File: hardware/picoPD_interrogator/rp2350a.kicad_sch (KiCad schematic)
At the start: 0 parts

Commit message: Added most of the RP2350A parts.
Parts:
- added C10, C11, C12: 4.7uF, Capacitor_SMD:C_0603_1608Metric, symbol Device:C
- added C13, C14, C15, C16, C17, C18, C19, C20, C21, C22: 100nF, Capacitor_SMD:C_0201_0603Metric, symbol Device:C
- added C8, C9: 15pF, Capacitor_SMD:C_0201_0603Metric, symbol Device:C
- added L2: 3.3uH, picoPD_interrogator:L_pol_2016, symbol Device:L
- added Q6: rohm-RE1C002UN, Package_TO_SOT_SMD:SOT-416, symbol picoPD_interrogator:rohm-RE1C002UN
- added R26, R27, R28, R29: 1K, Resistor_SMD:R_0201_0603Metric, symbol Device:R
- added R30, R31: 27R, Resistor_SMD:R_0201_0603Metric, symbol Device:R
- added R32: 33R, Resistor_SMD:R_0201_0603Metric, symbol Device:R
- added SW1, SW2: SW_Push, symbol Switch:SW_Push
- added U10: RP2350_60QFN, picoPD_interrogator:RP2350-QFN-60-1EP_7x7_P0.4mm_EP3.4x3.4mm_ThermalVias, symbol picoPD_interrogator:RP2350_60QFN
- added U11: W25Q128JVS, Package_SO:SOIC-8_5.23x5.23mm_P1.27mm, symbol Memory_Flash:W25Q128JVS
- added Y1: Crystal_GND24, Crystal:Crystal_SMD_Abracon_ABM10-4Pin_2.5x2.0mm, symbol Device:Crystal_GND24
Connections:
- new net: R31.2, U10.51 (USB_DM)
- new net: R30.2, U10.52 (USB_DP)
- new net: Q6.2 (S), R29.1, SW2.1
- new net: C8.1, R26.2, Y1.3
- new net: R27.1, SW1.1
- new net 1V1: C11.1, C13.1, C14.1, C15.1, L2.1, U10.23 (DVDD), U10.39 (DVDD), U10.50 (VREG_FB), U10.6 (DVDD)
- new net 3V3: C10.1, C16.1, C17.1, C18.1, C19.1, C20.1, C21.1, C22.1, R32.1, U10.1 (IOVDD), U10.11 (IOVDD), U10.20 (IOVDD), U10.30 (IOVDD), U10.38 (IOVDD), U10.44 (ADC_AVDD), U10.45 (IOVDD), U10.49 (VREG_VIN), U10.53 (USB_OTP_VDD), U10.54 (QSPI_IOVDD), U11.8 (VCC)
- new net 3V3_SMOOTHED: C12.1, R32.2, U10.46 (VREG_AVDD)
- new net FLASH_CLK: U10.56 (QSPI_SCLK), U11.6 (CLK)
- new net FLASH_DISABLE_L: R27.2, U10.60 (QSPI_SS), U11.1 (~{CS})
- new net FLASH_SD0: U10.57 (QSPI_SD0), U11.5 (DI(IO0))
- new net FLASH_SD1: U10.59 (QSPI_SD1), U11.2 (DO(IO1))
- new net FLASH_SD2: U10.58 (QSPI_SD2), U11.3 (IO2)
- new net FLASH_SD3: U10.55 (QSPI_SD3), U11.7 (IO3)
- new net GND: C10.2, C11.2, C12.2, C13.2, C14.2, C15.2, C16.2, C17.2, C18.2, C19.2, C20.2, C21.2, C22.2, C8.2, C9.2, R28.2, R29.2, SW1.2, U10.47 (VREG_PGND), U10.61 (GND), U11.4 (GND), Y1.4
- new net GP0: U10.2 (GPIO0)
- new net GP1: U10.3 (GPIO1)
- new net GP10: U10.14 (GPIO10)
- new net GP11: U10.15 (GPIO11)
- new net GP12: U10.16 (GPIO12)
- new net GP13: U10.17 (GPIO13)
- new net GP14: U10.18 (GPIO14)
- new net GP15: U10.19 (GPIO15)
- new net GP16: U10.27 (GPIO16)
- new net GP17: U10.28 (GPIO17)
- new net GP18: U10.29 (GPIO18)
- new net GP19: U10.31 (GPIO19)
- new net GP2: U10.4 (GPIO2)
- new net GP20: U10.32 (GPIO20)
- new net GP21: U10.33 (GPIO21)
- new net GP22: U10.34 (GPIO22)
- new net GP23: U10.35 (GPIO23)
- new net GP24: U10.36 (GPIO24)
- new net GP25: U10.37 (GPIO25)
- new net GP26_ADC0: U10.40 (GPIO26_ADC0)
- new net GP27_ADC1: U10.41 (GPIO27_ADC1)
- new net GP28_ADC2: U10.42 (GPIO28_ADC2)
- new net GP29_ADC3: U10.43 (GPIO29_ADC3)
- new net GP3: U10.5 (GPIO3)
- new net GP4: U10.7 (GPIO4)
- new net GP5: U10.8 (GPIO5)
- new net GP6: U10.9 (GPIO6)
- new net GP7: U10.10 (GPIO7)
- new net GP8: U10.12 (GPIO8)
- new net GP9: U10.13 (GPIO9)
- new net MCU_RESET_L: Q6.3 (D), SW2.2, U10.26 (RUN)
- new net RP2_RESET: Q6.1 (G), R28.1
- new net SWD_CLK: U10.24 (SWCLK)
- new net SWD_IO: U10.25 (SWD)
- new net USB_DM: R31.1
- new net USB_DP: R30.1
- new net VREG_LX: L2.2, U10.48 (VREG_LX)
- new net XIN: C9.1, U10.21 (XIN), Y1.1
- new net XOUT: R26.1, U10.22 (XOUT)
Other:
- note added: "RP2 Reset Button"
- note added: "USB Bootloader Button"

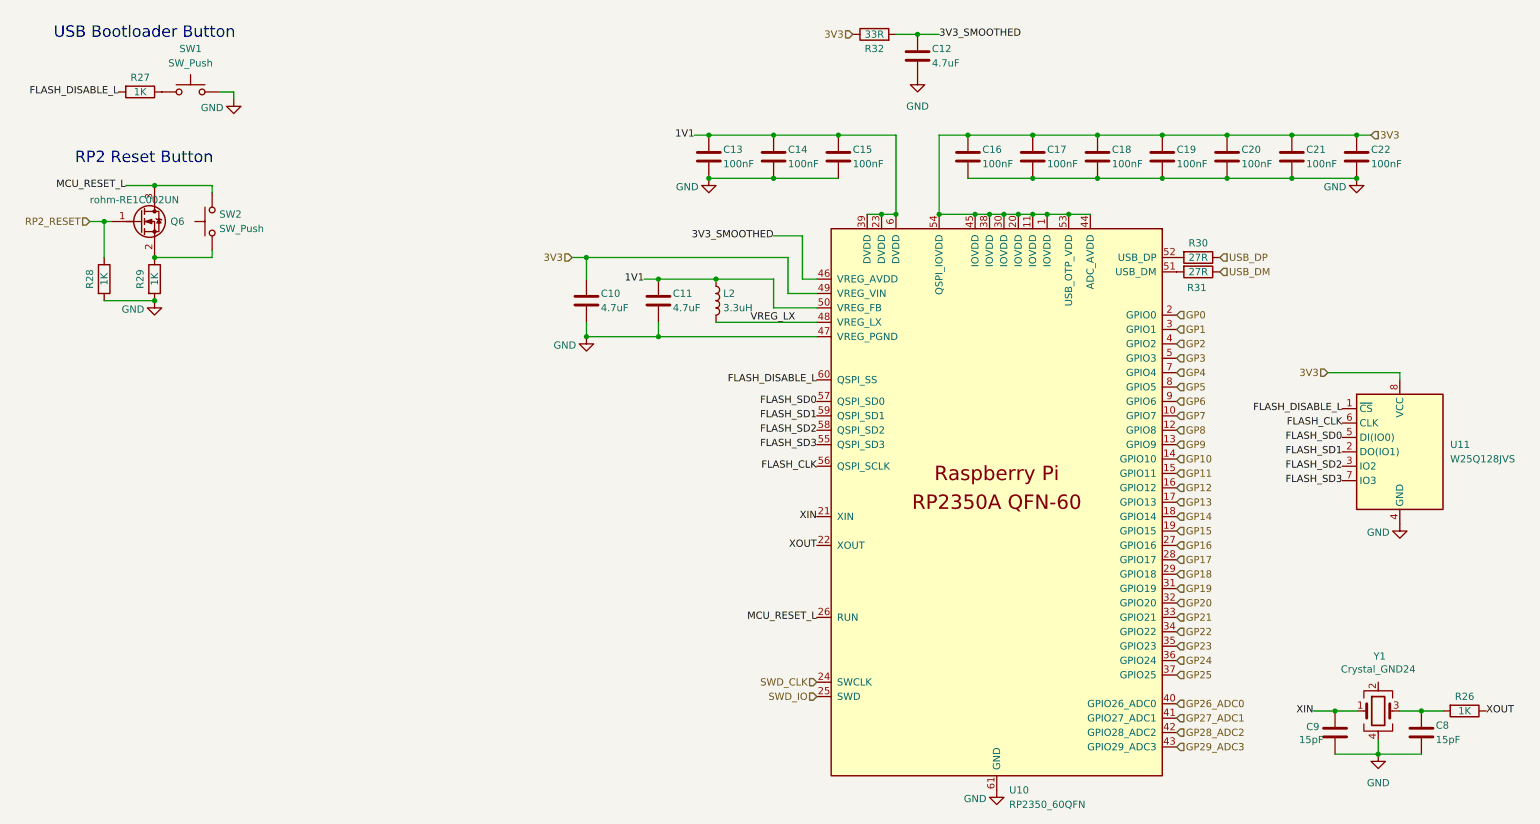
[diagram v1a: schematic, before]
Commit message: Schematic: Added QWIIC Connector. Changed 56K Rp resistor to 35K since we are pulling up 3.3v instead of 5v.
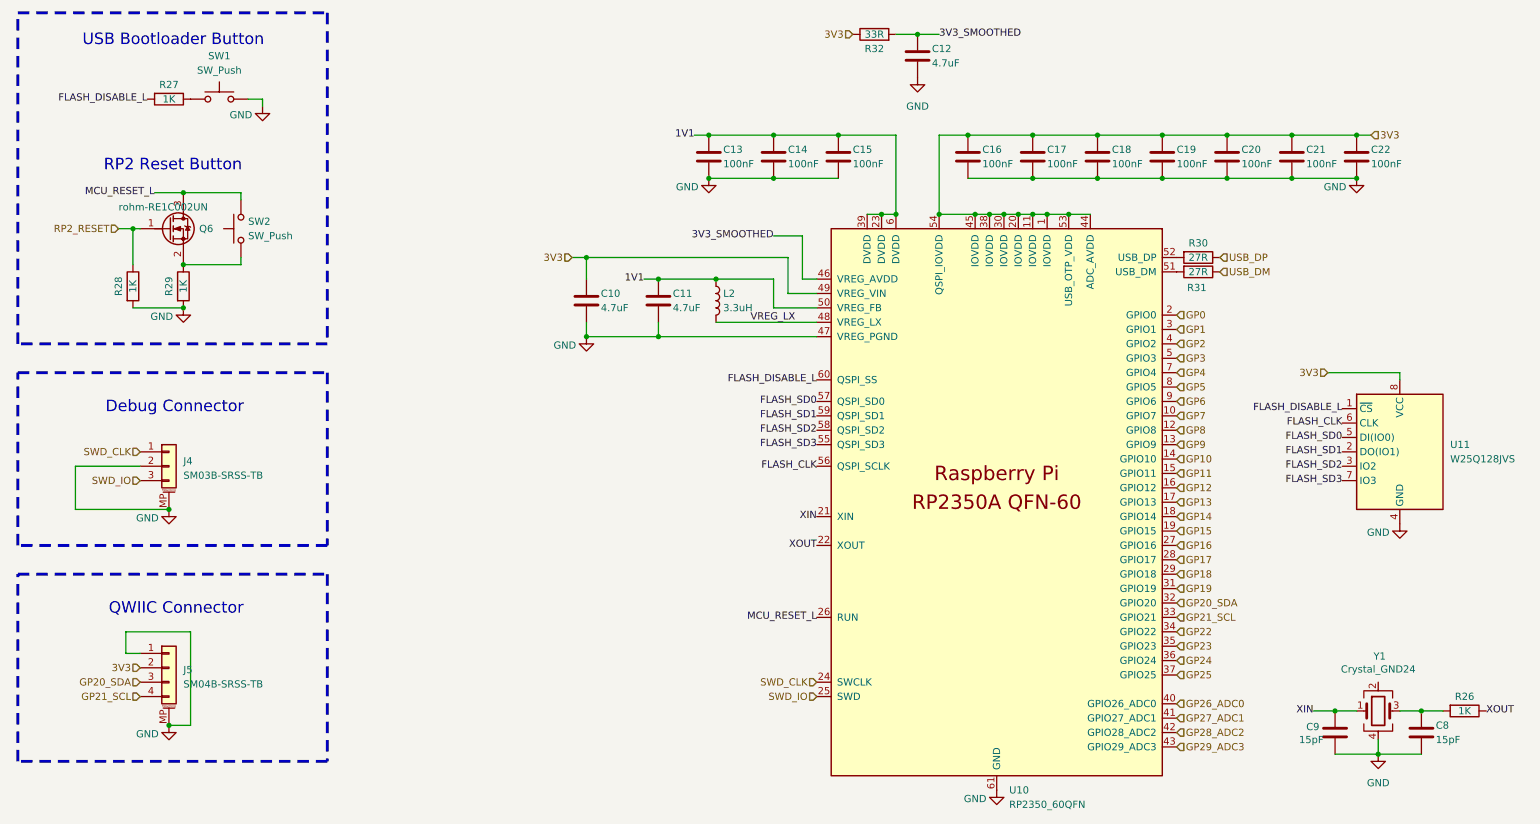
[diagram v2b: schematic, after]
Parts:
- added J4: SM03B-SRSS-TB, Connector_JST:JST_SH_SM03B-SRSS-TB_1x03-1MP_P1.00mm_Horizontal, symbol Connector_Generic_MountingPin:Conn_01x03_MountingPin
- added J5: SM04B-SRSS-TB, Connector_JST:JST_SH_SM04B-SRSS-TB_1x04-1MP_P1.00mm_Horizontal, symbol Connector_Generic_MountingPin:Conn_01x04_MountingPin
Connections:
- net 3V3: now also J5.2 (Pin_2)
- net GND: now also J4.2 (Pin_2), J4.MP (MountPin), J5.1 (Pin_1), J5.MP (MountPin)
- net SWD_CLK: now also J4.1 (Pin_1)
- net SWD_IO: now also J4.3 (Pin_3)
- net GP20 renamed GP20_SDA
- net GP20_SDA: now also J5.3 (Pin_3)
- net GP21 renamed GP21_SCL
- net GP21_SCL: now also J5.4 (Pin_4)
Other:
- note added: "Debug Connector"
- note added: "QWIIC Connector"
- moved on the sheet: Q6, R27, R28, R29, SW1, SW2

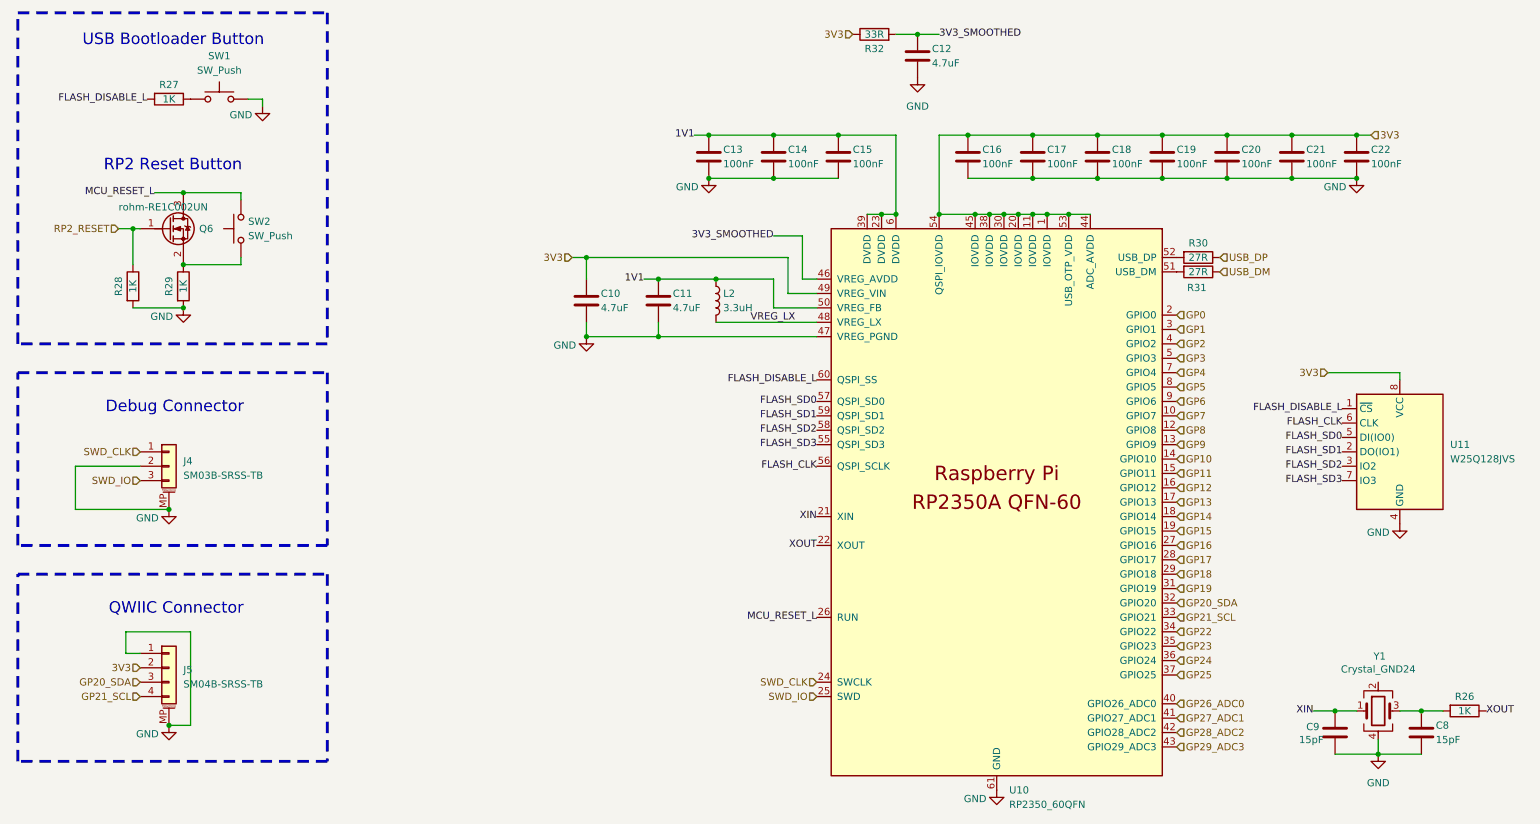
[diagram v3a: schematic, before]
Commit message: Schematic: Added an 'Extra Pins' connector.
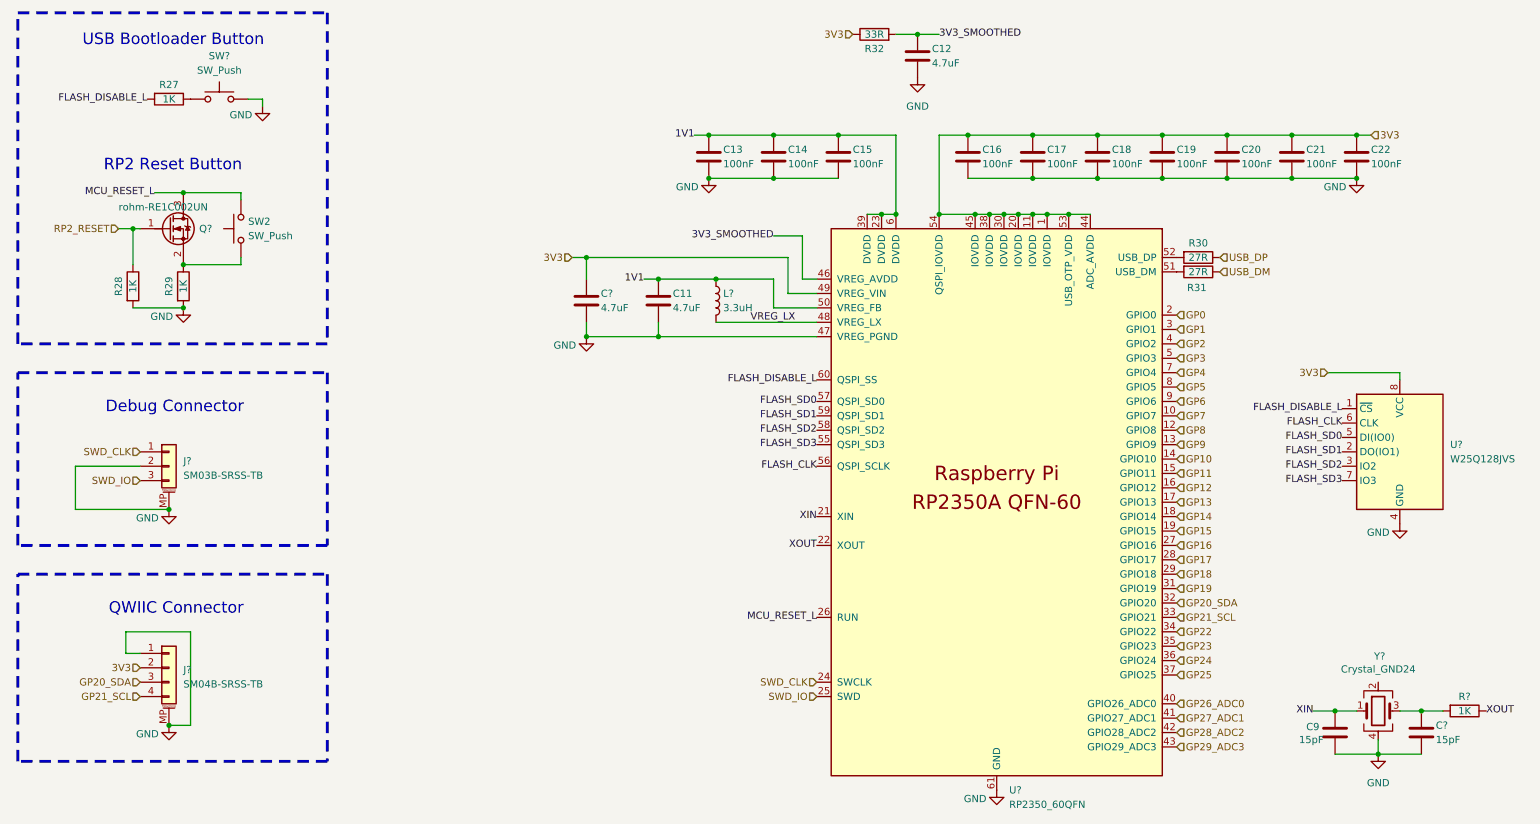
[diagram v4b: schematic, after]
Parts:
- renumbered C8 to C?, C10 to C?, J4 to J?, J5 to J?, L2 to L?, Q6 to Q?, R26 to R?, SW1 to SW?, U10 to U?, U11 to U?, Y1 to Y?
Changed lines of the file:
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@@
 		(dnp no)
 		(fields_autoplaced yes)
-		(property "Reference" "U10"
+		(property "Reference" "U?"
 			(at 191.4241 153.67 0)
 			(effects
@@
 		(pin "60"
 		)
+		(instances
+			(project "picoPD_interrogator"
+				(path "/e34b0978-7def-4921-94d0-accc0a677529/dcdf1db7-f9f6-495b-a623-7e4b73e77f06"
+					(reference "U?")
+					(unit 1)
+				)
+			)
+		)
 	)
 	(symbol
@@
 		(dnp no)
 		(fields_autoplaced yes)
-		(property "Reference" "U11"
+		(property "Reference" "U?"
 			(at 269.24 92.7099 0)
 			(effects
@@
 		(pin "7"
 		)
+		(instances
+			(project "picoPD_interrogator"
+				(path "/e34b0978-7def-4921-94d0-accc0a677529/dcdf1db7-f9f6-495b-a623-7e4b73e77f06"
+					(reference "U?")
+					(unit 1)
+				)
+			)
+		)
 	)
 	(symbol
@@
 		(on_board yes)
 		(dnp no)
-		(property "Reference" "Y1"
+		(property "Reference" "Y?"
 			(at 256.794 130.048 0)
 			(effects
@@
 		(pin "3"
 		)
+		(instances
+			(project "picoPD_interrogator"
+				(path "/e34b0978-7def-4921-94d0-accc0a677529/dcdf1db7-f9f6-495b-a623-7e4b73e77f06"
+					(reference "Y?")
+					(unit 1)
+				)
+			)
+		)
 	)
 	(symbol
@@
 		(dnp no)
 		(fields_autoplaced yes)
-		(property "Reference" "#PWR036"
+		(property "Reference" "#PWR?"
 			(at 175.26 34.29 0)
 			(effects
@@
 		(pin "1"
 		)
+		(instances
+			(project "picoPD_interrogator"
+				(path "/e34b0978-7def-4921-94d0-accc0a677529/dcdf1db7-f9f6-495b-a623-7e4b73e77f06"
+					(reference "#PWR?")
+					(unit 1)
+				)
+			)
+		)
 	)
 	(symbol
@@
 		(dnp no)
 		(fields_autoplaced yes)
-		(property "Reference" "#PWR031"
+		(property "Reference" "#PWR?"
 			(at 256.54 153.67 0)
 			(effects
@@
 		(pin "1"
 		)
+		(instances
+			(project "picoPD_interrogator"
+				(path "/e34b0978-7def-4921-94d0-accc0a677529/dcdf1db7-f9f6-495b-a623-7e4b73e77f06"
+					(reference "#PWR?")
+					(unit 1)
+				)
+			)
+		)
 	)
 	(symbol
@@
 		(dnp no)
 		(fields_autoplaced yes)
-		(property "Reference" "SW1"
+		(property "Reference" "SW?"
 			(at 52.07 24.13 0)
 			(effects
@@
 		(pin "2"
 		)
+		(instances
+			(project "picoPD_interrogator"
+				(path "/e34b0978-7def-4921-94d0-accc0a677529/dcdf1db7-f9f6-495b-a623-7e4b73e77f06"
+					(reference "SW?")
+					(unit 1)
+				)
+			)
+		)
 	)
 	(symbol
@@
 		(dnp no)
 		(fields_autoplaced yes)
-		(property "Reference" "J4"
+		(property "Reference" "J?"
 			(at 45.72 95.6055 0)
 			(effects
@@
 		(pin "2"
 		)
+		(instances
+			(project "picoPD_interrogator"
+				(path "/e34b0978-7def-4921-94d0-accc0a677529/dcdf1db7-f9f6-495b-a623-7e4b73e77f06"
+					(reference "J?")
+					(unit 1)
+				)
+			)
+		)
 	)
 	(symbol
@@
 		(on_board yes)
 		(dnp no)
-		(property "Reference" "#PWR032"
+		(property "Reference" "#PWR?"
 			(at 59.69 39.37 0)
 			(effects
@@
 		(pin "1"
 		)
+		(instances
+			(project "picoPD_interrogator"
+				(path "/e34b0978-7def-4921-94d0-accc0a677529/dcdf1db7-f9f6-495b-a623-7e4b73e77f06"
+					(reference "#PWR?")
+					(unit 1)
+				)
+			)
+		)
 	)
 	(symbol
@@
 		(on_board yes)
 		(dnp no)
-		(property "Reference" "C8"
+		(property "Reference" "C?"
 			(at 266.7 142.24 0)
 			(effects
@@
 		(pin "2"
 		)
+		(instances
+			(project "picoPD_interrogator"
+				(path "/e34b0978-7def-4921-94d0-accc0a677529/dcdf1db7-f9f6-495b-a623-7e4b73e77f06"
+					(reference "C?")
+					(unit 1)
+				)
+			)
+		)
 	)
 	(symbol
@@
 		(on_board yes)
 		(dnp no)
-		(property "Reference" "Q6"
+		(property "Reference" "Q?"
 			(at 48.514 54.61 0)
 			(effects
@@
 		(pin "2"
 		)
+		(instances
+			(project "picoPD_interrogator"
+				(path "/e34b0978-7def-4921-94d0-accc0a677529/dcdf1db7-f9f6-495b-a623-7e4b73e77f06"
+					(reference "Q?")
+					(unit 1)
+				)
+			)
+		)
 	)
 	(symbol
@@
 		(on_board yes)
 		(dnp no)
-		(property "Reference" "R26"
+		(property "Reference" "R?"
 			(at 271.78 137.16 90)
 			(effects
@@
 		)
 		(pin "1"
+		)
+		(instances
+			(project "picoPD_interrogator"
+				(path "/e34b0978-7def-4921-94d0-accc0a677529/dcdf1db7-f9f6-495b-a623-7e4b73e77f06"
+					(reference "R?")
+					(unit 1)
+				)
+			)
 		)
 	)
@@
 		(dnp no)
 		(fields_autoplaced yes)
-		(property "Reference" "L2"
+		(property "Reference" "L?"
 			(at 140.97 66.0399 0)
 			(effects
@@
 		(pin "1"
 		)
+		(instances
+			(project "picoPD_interrogator"
+				(path "/e34b0978-7def-4921-94d0-accc0a677529/dcdf1db7-f9f6-495b-a623-7e4b73e77f06"
+					(reference "L?")
+					(unit 1)
+				)
+			)
+		)
 	)
 	(symbol
@@
 		(on_board yes)
 		(dnp no)
-		(property "Reference" "C10"
+		(property "Reference" "C?"
 			(at 119.38 66.04 0)
 			(effects
@@
 		(pin "2"
 		)
+		(instances
+			(project "picoPD_interrogator"
+				(path "/e34b0978-7def-4921-94d0-accc0a677529/dcdf1db7-f9f6-495b-a623-7e4b73e77f06"
+					(reference "C?")
+					(unit 1)
+				)
+			)
+		)
 	)
 	(symbol
@@
 		(dnp no)
 		(fields_autoplaced yes)
-		(property "Reference" "J5"
+		(property "Reference" "J?"
 			(at 45.72 132.4355 0)
 			(effects
@@
 		(pin "1"
 		)
-	)
+		(instances
+			(project "picoPD_interrogator"
+				(path "/e34b0978-7def-4921-94d0-accc0a677529/dcdf1db7-f9f6-495b-a623-7e4b73e77f06"
+					(reference "J?")
+					(unit 1)
+				)
+			)
+		)
+	)
